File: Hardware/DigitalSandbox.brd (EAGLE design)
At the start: 109.2 x 76.2 mm, 82 parts, among them Q1 MOSFET-N, Q2 MOSFET-P, Q3 MOSFET-N, Q4 MOSFET-N, Q5 MOSFET-N, U1 MCP73831, U2 ATMEGA328, U3 C2031N-1A2-B10K-GP, U4 MCP9700, U5 FT232RLSSOP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

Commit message: Changes Made: 1. Swap Tx-Rx 3. correct stop mask on 2 exposed vias 6. flip default logic for push button (Currently normally high) 9. Change i2c header to meet new standard in the works.
TODO:
2. Make programming vias for Production
4. reverse the direction of the potentiometer and add silk showing "0 - 1024"
5. Source new push button
7. Investigate adding pulldown resistors for the nchannel fets that service the RGB led
8. Investigate a new resistor value for the light sensor to increase sensitivity.
10. Label pin 13 LED (near the uC).
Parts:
- turned S4 to 180 degrees
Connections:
- removed net RXI: U2.30, U5.5
- removed net TXO: U2.31, U5.1
- new net RXD: U2.30, U5.1
- new net TXD: U2.31, U5.5
- net D12: now also R23.2, S4.1, S4.2; no longer R23.1, S4.3, S4.4
- net GND: now also R23.1; no longer S4.1, S4.2
- net VCC: now also S4.3, S4.4; no longer R23.2
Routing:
- net TXD: track 0.00 -> 14.7 mm, vias 0 -> 2
- net RXI: track 14.1 -> 0.00 mm, vias 2 -> 0
- net TXO: track 11.5 -> 0.00 mm
- net RXD: track 0.00 -> 10.8 mm
- net VCC: track 400.5 -> 403.6 mm
- net D12: track 171.3 -> 173.9 mm

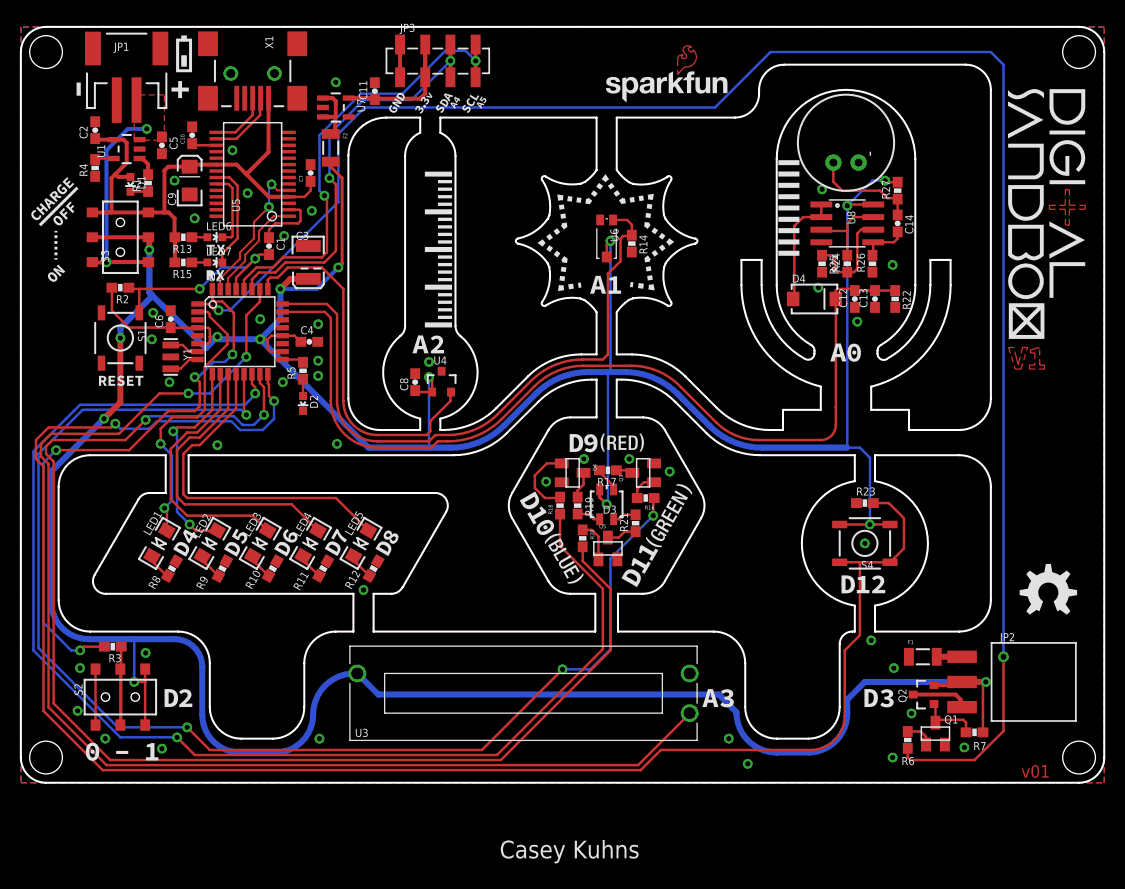
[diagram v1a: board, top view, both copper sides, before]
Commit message: Changes Made
1. Made programming vias for Production
2. reversed the direction of the potentiometer and added silk showing "0 - 1024"
3. Replaced Mosfets with NPN transistors to control RGB led
4. Replaces Light sensor with one used on Weather Shield IC-11836
5. Labeled pin 13 LED (near the uC).

TODO
1. Source new push button with better tactile feedback
2. Source new RGB Led that is diffused and common cathode (this would eliminate the need for transistors.
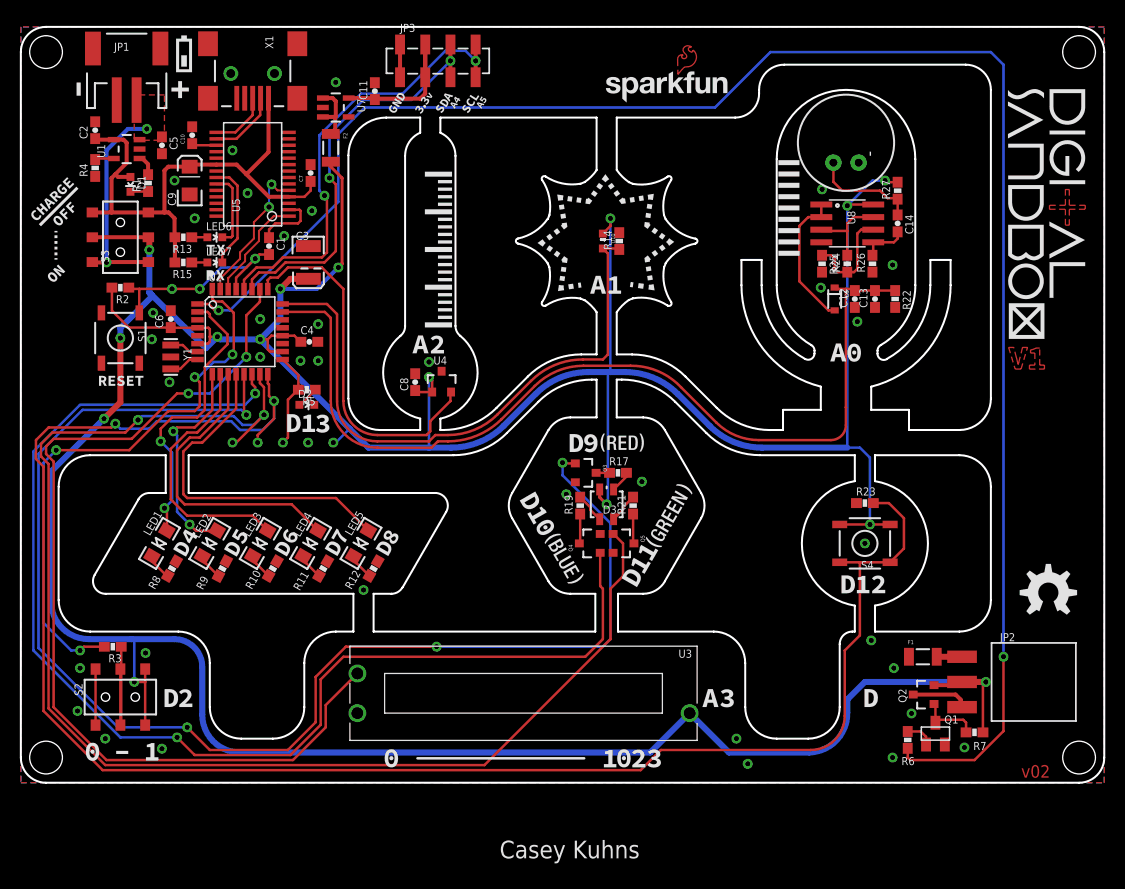
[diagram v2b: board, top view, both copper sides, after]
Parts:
- removed D4: MBRA140, SparkFun:SMA-DIODE
- removed R16, R18, R20: 1k, SparkFun-Passives:0603-RES
- removed U6: TEMT6000, SparkFun:TEMT6000-SEN
- added D5: (no value), SparkFun-DiscreteSemi:SOD-323
- added U10: LIGHTSENSORALS, SparkFun-Sensors:ALS-PT19
- Q3, Q4, Q5: value MOSFET-N -> MMBT2222A; device SparkFun-DiscreteSemi:SOT23 -> SparkFun-DiscreteSemi:SOT23-3
- moved Q4 7.33 mm to (57.4, 24.1), turned to 90 degrees
- moved Q3 5.84 mm to (56.9, 31.2), turned to 270 degrees
- moved R5 1.94 mm to (28.8, 39.6), turned to 180 degrees
- moved R21 1.80 mm to (61.7, 27.9)
- moved Q5 1.61 mm to (60.7, 24.1), turned to 270 degrees
- moved R14 1.30 mm to (60.3, 54.6), turned to 90 degrees
- moved R17 1.05 mm to (60.2, 31.2), turned to 0 degrees
- moved D2 0.40 mm to (28.8, 38.1), turned to 270 degrees
- moved R19 0.25 mm to (56.4, 27.9), turned to 90 degrees
- turned U3 to 0 degrees
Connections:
- removed net N$14: Q3.1, R16.2
- removed net N$19: Q4.1, R18.2
- removed net N$22: Q5.1, R20.1
- net A0: now also D5.1; no longer D4.C
- net A1: now also U10.E; no longer U6.EMITTER
- net D10: now also Q4.1; no longer R18.1
- net D11: now also Q5.1; no longer R20.2
- net D9: now also Q3.1; no longer R16.1
- net N$24: now also D5.2; no longer D4.A
- net VCC: now also U10.C; no longer U6.COLLECTOR
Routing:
- net A3: track 127.8 -> 96.2 mm
- net N$19: track 7.53 -> 0.00 mm
- net D13: track 2.34 -> 9.70 mm, vias 0 -> 1
- net D9: track 129.9 -> 137.1 mm
- net D11: track 129.2 -> 135.8 mm, vias 2 -> 3
- net D12: track 173.9 -> 178.7 mm, vias 2 -> 3
- net N$22: track 4.17 -> 0.00 mm
- net A1: track 63.0 -> 59.0 mm
- net D10: track 128.7 -> 125.2 mm
- net N$14: track 2.90 -> 0.00 mm
- net N$24: track 11.8 -> 14.2 mm
- net VCC: track 403.6 -> 404.9 mm, vias 15 -> 16
- net A0: track 91.4 -> 92.7 mm
- net GRN: track 2.41 -> 3.04 mm
- net N$28: track 2.44 -> 3.04 mm
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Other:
- board text added: "GND"
- board text added: "MISO"
- board text added: "MOSI"
- board text added: "RST"
- board text added: "SCK"
- board text added: "VCC"
- board text added: "v02"
- board text removed: "v01"

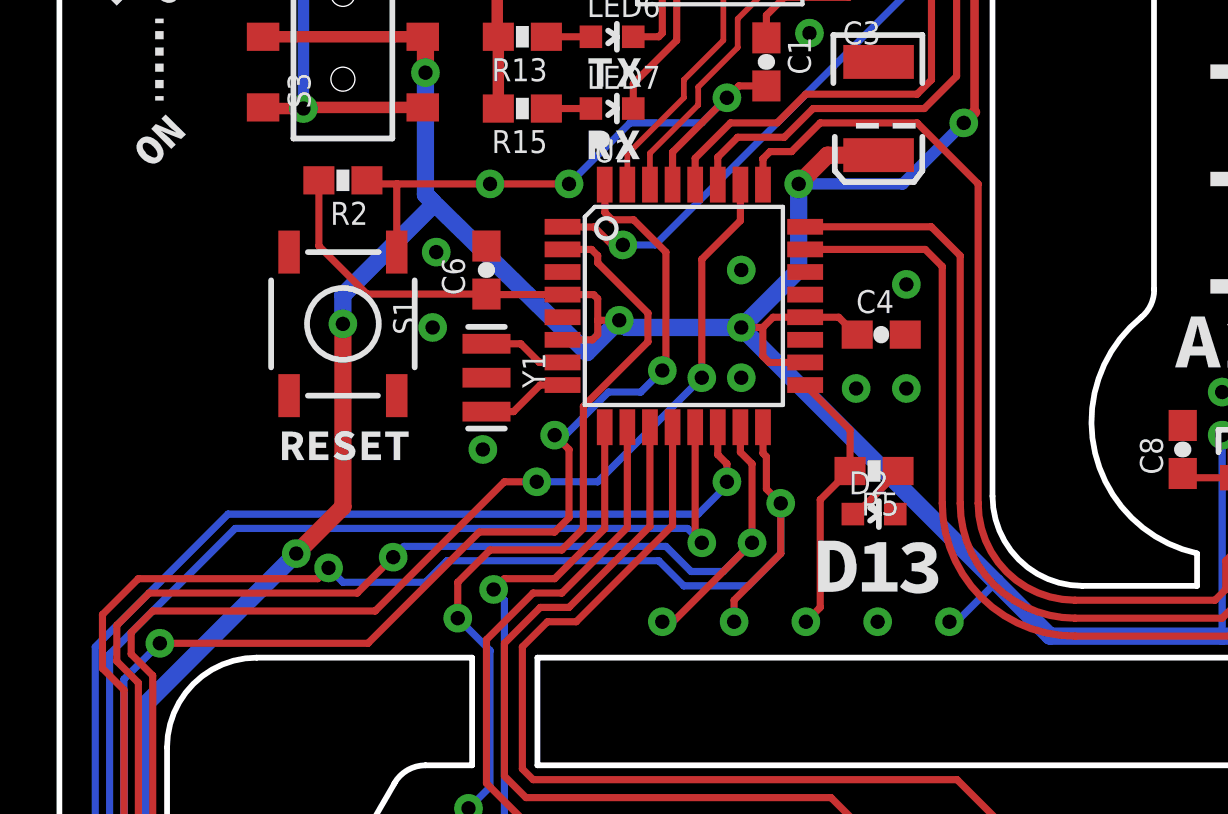
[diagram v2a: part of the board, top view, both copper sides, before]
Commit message: added ISP header
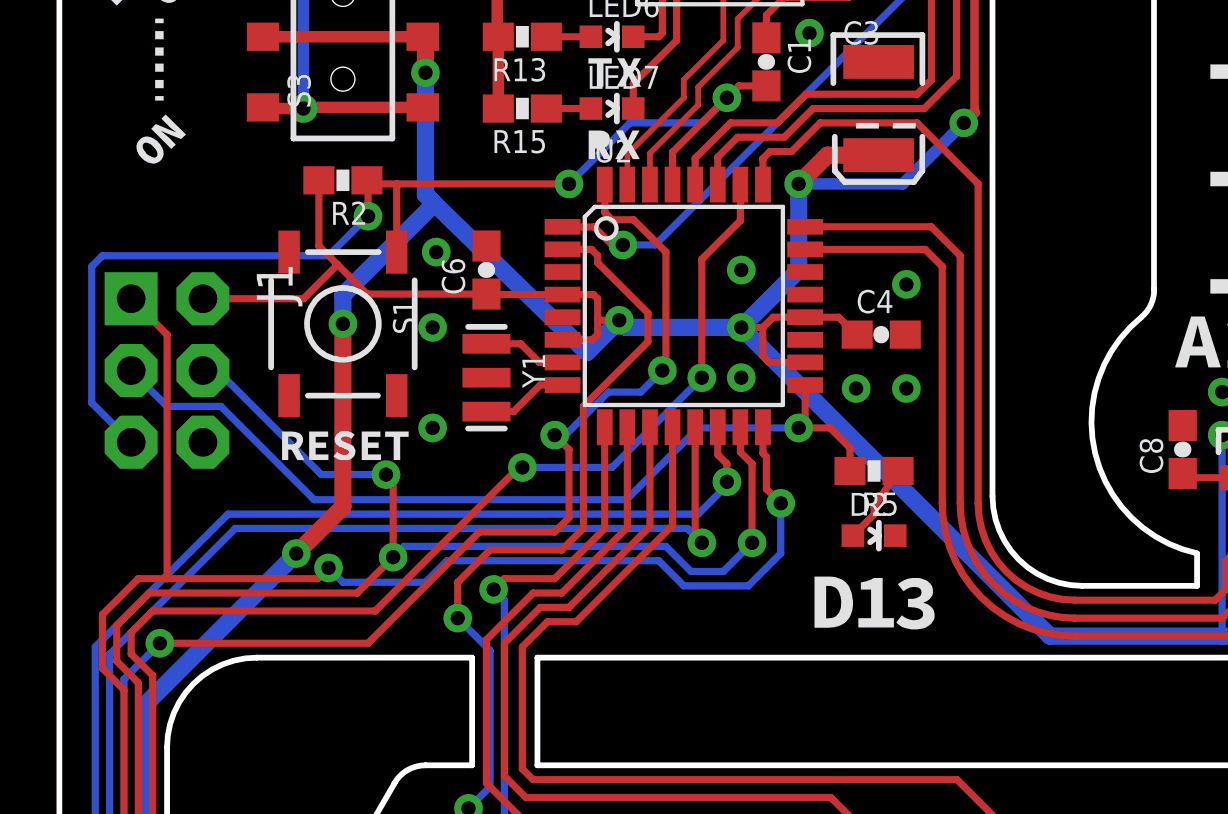
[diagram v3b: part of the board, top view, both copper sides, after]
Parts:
- added J1: AVR_SPI_PRG_6NS, SparkFun-Connectors:2X3-NS
- moved D2 0.76 mm to (28.8, 37.3)
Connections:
- net D11: now also J1.4
- net D12: now also J1.1
- net D13: now also J1.3
- net GND: now also J1.6
- net RST: now also J1.5
- net VCC: now also J1.2
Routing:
- net D13: track 9.70 -> 31.1 mm
- net RST: track 21.9 -> 40.5 mm
- net D11: track 135.8 -> 142.5 mm
- net D12: track 178.7 -> 184.3 mm, vias 3 -> 2
- net VCC: track 404.9 -> 407.9 mm, vias 16 -> 15
- net N$2: track 2.25 -> 2.85 mm
- net GND: vias 37 -> 36
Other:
- board text removed: "GND"
- board text removed: "MISO"
- board text removed: "MOSI"
- board text removed: "RST"
- board text removed: "SCK"
- board text removed: "VCC"
